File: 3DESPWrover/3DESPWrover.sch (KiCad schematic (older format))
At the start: 21 parts, among them J1 Conn_01x05_Male, J2 Conn_01x03_Female, J3 Conn_02x03_Odd_Even, J4 Conn_02x07_Odd_Even, SW1 SW_Push, SW2 SW_Push, U1 ESP32-S2-WROVER

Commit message: Cleared Andres comments
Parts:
- added NT1: Net-Tie_2, NetTie:NetTie-2_SMD_Pad0.5mm, symbol Device:Net-Tie_2
- added R4: 10k, Resistor_SMD:R_0805_2012Metric_Pad1.20x1.40mm_HandSolder, symbol Device:R
- C10, C9: Voltage (none) -> 10V
- C11: Voltage (none) -> 50V
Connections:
- net +3V3: now also NT1.2, R4.2
- net AD1: now also R4.1
- net D6: now also J3.3 (Pin_3); no longer J3.2 (Pin_2)
- net GND: now also J3.2 (Pin_2); no longer J3.5 (Pin_5)
- net Vin: now also J3.5 (Pin_5); no longer J3.3 (Pin_3)
- net Vout: now also NT1.1
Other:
- note added: "K78L03-500R3 DC-DC Converter\nVin: 4.75-30V"
- note removed: "K78L03-500R3 DC-DC Converter\nVin: 4.75-36V"
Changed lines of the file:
@@
 F 1 "ESP32-S2-WROVER" H 1700 3540 50  0000 C CNN
 F 2 "RF_Module:ESP32-S2-WROVER" H 2450 1100 50  0001 C CNN
-F 3 "https://www.espressif.com/sites/default/files/documentation/esp32-s2-wroom_esp32-s2-wroom-i_datasheet_en.pdf" H 1400 1450 50  0001 C CNN
+F 3 "https://www.espressif.com/sites/default/files/documentation/esp32-s2-wrover_esp32-s2-wrover-i_datasheet_en.pdf" H 1400 1450 50  0001 C CNN
 	1    1700 2250
 	1    0    0    -1
@@
 	1100 3050 750  3050
 Wire Wire Line
-	1100 3150 750  3150
+	1100 3150 950  3150
 $Comp
 L power:GND #PWR01
@@
 F 2 "Capacitor_SMD:C_0805_2012Metric_Pad1.18x1.45mm_HandSolder" H 9738 1850 50  0001 C CNN
 F 3 "~" H 9700 2000 50  0001 C CNN
+F 4 "10V" H 9700 2000 50  0000 C CNN "Voltage"
 	1    9700 2000
 	1    0    0    -1
@@
 F 2 "Capacitor_SMD:C_0805_2012Metric_Pad1.18x1.45mm_HandSolder" H 10388 1850 50  0001 C CNN
 F 3 "~" H 10350 2000 50  0001 C CNN
+F 4 "10V" H 10350 2000 50  0000 C CNN "Voltage"
 	1    10350 2000
 	1    0    0    -1
@@
 F 2 "Capacitor_SMD:C_0805_2012Metric_Pad1.18x1.45mm_HandSolder" H 10988 1850 50  0001 C CNN
 F 3 "~" H 10950 2000 50  0001 C CNN
+F 4 "50V" H 10950 2000 50  0000 C CNN "Voltage"
 	1    10950 2000
 	1    0    0    -1
@@
 $EndComp
 Wire Wire Line
-	9700 1700 9850 1700
+	9700 1700 9800 1700
 Connection ~ 9700 1700
 Wire Wire Line
-	10150 1700 10350 1700
+	10150 1700 10250 1700
 Text Label 9450 1700 0    50   ~ 0
 Vout
@@
 ESP32-S2 WROVER\nModule
 Text Notes 9750 700  0    50   ~ 0
-K78L03-500R3 DC-DC Converter\nVin: 4.75-36V
+K78L03-500R3 DC-DC Converter\nVin: 4.75-30V
 $Comp
 L power:+3.3V #PWR024
@@
 Text Label 6550 3550 0    50   ~ 0
 D5
-Text Label 6550 3450 0    50   ~ 0
+Text Label 5700 3550 0    50   ~ 0
 D6
 Text Label 7350 3350 0    50   ~ 0
@@
 	1    0    0    -1
 $EndComp
-$Comp
-L power:GND #PWR014
-U 1 1 61BB5847
-P 5600 3750
-F 0 "#PWR014" H 5600 3500 50  0001 C CNN
-F 1 "GND" H 5605 3577 50  0000 C CNN
-F 2 "" H 5600 3750 50  0001 C CNN
-F 3 "" H 5600 3750 50  0001 C CNN
-	1    5600 3750
-	1    0    0    -1
-$EndComp
-Wire Wire Line
-	5850 3650 5600 3650
-Wire Wire Line
-	5600 3650 5600 3750
 Wire Wire Line
 	6350 3650 6600 3650
@@
 	7600 3350 7350 3350
 Wire Wire Line
-	6350 3450 6550 3450
-Wire Wire Line
-	5850 3550 5600 3550
-Wire Wire Line
-	5600 3550 5600 3450
+	8350 2950 8550 2950
+Wire Wire Line
+	8350 2950 8350 3250
+Wire Wire Line
+	7300 2950 7100 2950
+Wire Wire Line
+	7300 2950 7300 3250
+$Comp
+L Device:R R4
+U 1 1 61C33742
+P 950 3550
+F 0 "R4" H 1020 3596 50  0000 L CNN
+F 1 "10k" H 1020 3505 50  0000 L CNN
+F 2 "Resistor_SMD:R_0805_2012Metric_Pad1.20x1.40mm_HandSolder" V 880 3550 50  0001 C CNN
+F 3 "~" H 950 3550 50  0001 C CNN
+	1    950  3550
+	1    0    0    -1
+$EndComp
+Wire Wire Line
+	950  3400 950  3150
+Connection ~ 950  3150
+Wire Wire Line
+	950  3150 750  3150
+$Comp
+L power:+3.3V #PWR029
+U 1 1 61C379CF
+P 750 3800
+F 0 "#PWR029" H 750 3650 50  0001 C CNN
+F 1 "+3.3V" H 765 3973 50  0000 C CNN
+F 2 "" H 750 3800 50  0001 C CNN
+F 3 "" H 750 3800 50  0001 C CNN
+	1    750  3800
+	1    0    0    -1
+$EndComp
+Wire Wire Line
+	950  3700 950  3900
+Wire Wire Line
+	950  3900 750  3900
+Wire Wire Line
+	750  3900 750  3800
+$Comp
+L Device:Net-Tie_2 NT1
+U 1 1 61C3CDD7
+P 10050 1400
+F 0 "NT1" H 10050 1581 50  0000 C CNN
+F 1 "Net-Tie_2" H 10050 1490 50  0000 C CNN
+F 2 "NetTie:NetTie-2_SMD_Pad0.5mm" H 10050 1400 50  0001 C CNN
+F 3 "~" H 10050 1400 50  0001 C CNN
+	1    10050 1400
+	1    0    0    -1
+$EndComp
+Wire Wire Line
+	9950 1400 9850 1400
+Wire Wire Line
+	9850 1400 9850 1550
+Wire Wire Line
+	9850 1550 9800 1550
+Wire Wire Line
+	9800 1550 9800 1700
+Connection ~ 9800 1700
+Wire Wire Line
+	9800 1700 9850 1700
+Wire Wire Line
+	10150 1400 10250 1400
+Wire Wire Line
+	10250 1400 10250 1700
+Connection ~ 10250 1700
+Wire Wire Line
+	10250 1700 10350 1700
+Wire Wire Line
+	5850 3650 5600 3650
+Wire Wire Line
+	5600 3650 5600 3450
 Connection ~ 5600 3450
 Wire Wire Line
-	8350 2950 8550 2950
-Wire Wire Line
-	8350 2950 8350 3250
-Wire Wire Line
-	7300 2950 7100 2950
-Wire Wire Line
-	7300 2950 7300 3250
+	5850 3550 5700 3550
+Wire Wire Line
+	6350 3450 6750 3450
+Wire Wire Line
+	6750 3450 6750 3650
+Wire Wire Line
+	6750 3650 6600 3650
+Connection ~ 6600 3650
 $EndSCHEMATC

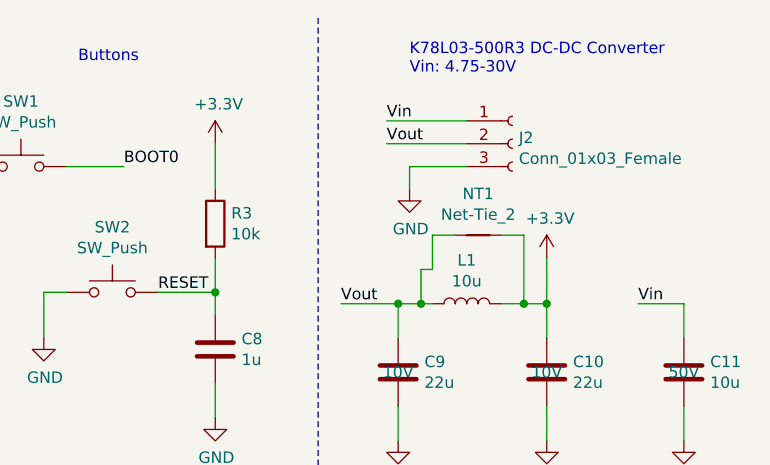
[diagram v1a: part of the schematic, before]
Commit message: Correction to 3.3v regulator connection
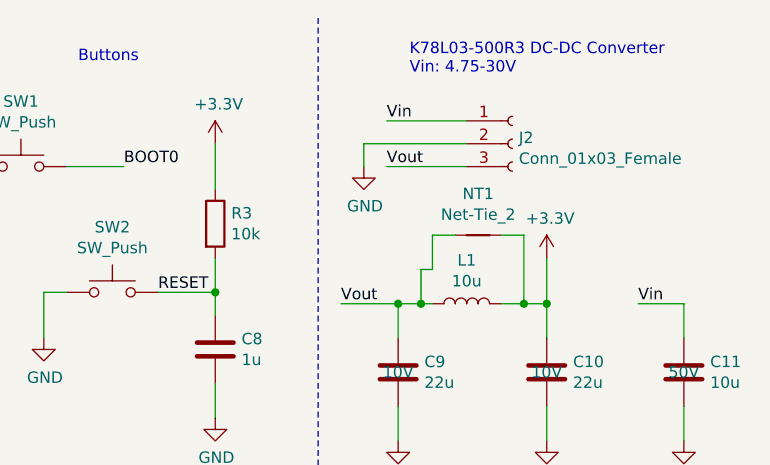
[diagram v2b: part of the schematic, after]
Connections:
- net GND: now also J2.2 (Pin_2); no longer J2.3 (Pin_3)
- net Vout: now also J2.3 (Pin_3); no longer J2.2 (Pin_2)
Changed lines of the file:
@@
 Vin
 Wire Wire Line
-	10000 1000 9650 1000
-Text Label 9650 1000 0    50   ~ 0
+	10000 1100 9650 1100
+Text Label 9650 1100 0    50   ~ 0
 Vout
 $Comp
 L power:GND #PWR023
 U 1 1 61BD0ED8
-P 9750 1200
-F 0 "#PWR023" H 9750 950 50  0001 C CNN
-F 1 "GND" H 9755 1027 50  0000 C CNN
-F 2 "" H 9750 1200 50  0001 C CNN
-F 3 "" H 9750 1200 50  0001 C CNN
-	1    9750 1200
+P 9550 1100
+F 0 "#PWR023" H 9550 850 50  0001 C CNN
+F 1 "GND" H 9555 927 50  0000 C CNN
+F 2 "" H 9550 1100 50  0001 C CNN
+F 3 "" H 9550 1100 50  0001 C CNN
+	1    9550 1100
 	1    0    0    -1
 $EndComp
 Wire Wire Line
-	10000 1100 9750 1100
+	10000 1000 9550 1000
 Wire Wire Line
-	9750 1100 9750 1200
+	9550 1000 9550 1100
 $Comp
 L Device:C C9
